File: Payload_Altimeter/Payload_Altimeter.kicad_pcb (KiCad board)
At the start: 2 copper layers, 80 x 93.6 mm, 6 parts, among them J1 L717SDC37P1ACH4F, J2 Conn_02x20_Odd_Even, U7 MS5607-02BA

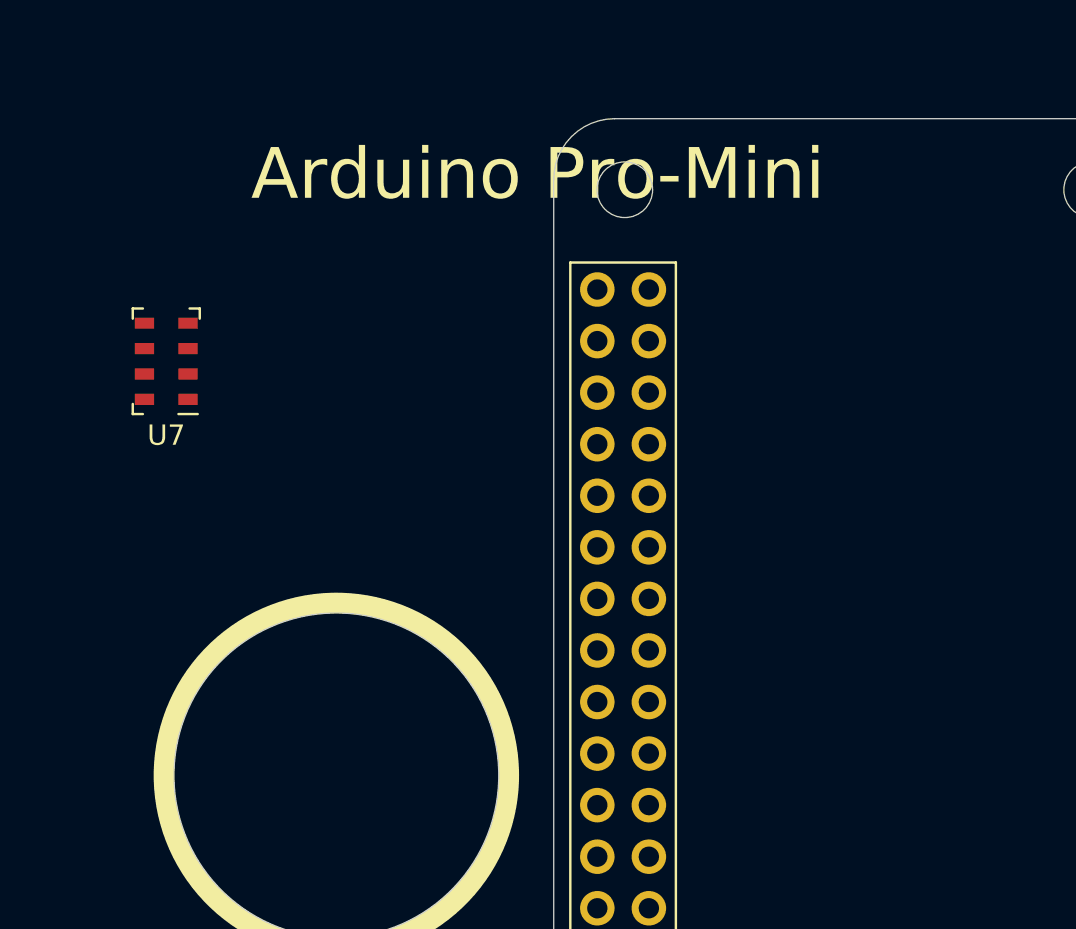
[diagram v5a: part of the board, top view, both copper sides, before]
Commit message: Some connection
Put some of the connections on but not all of them
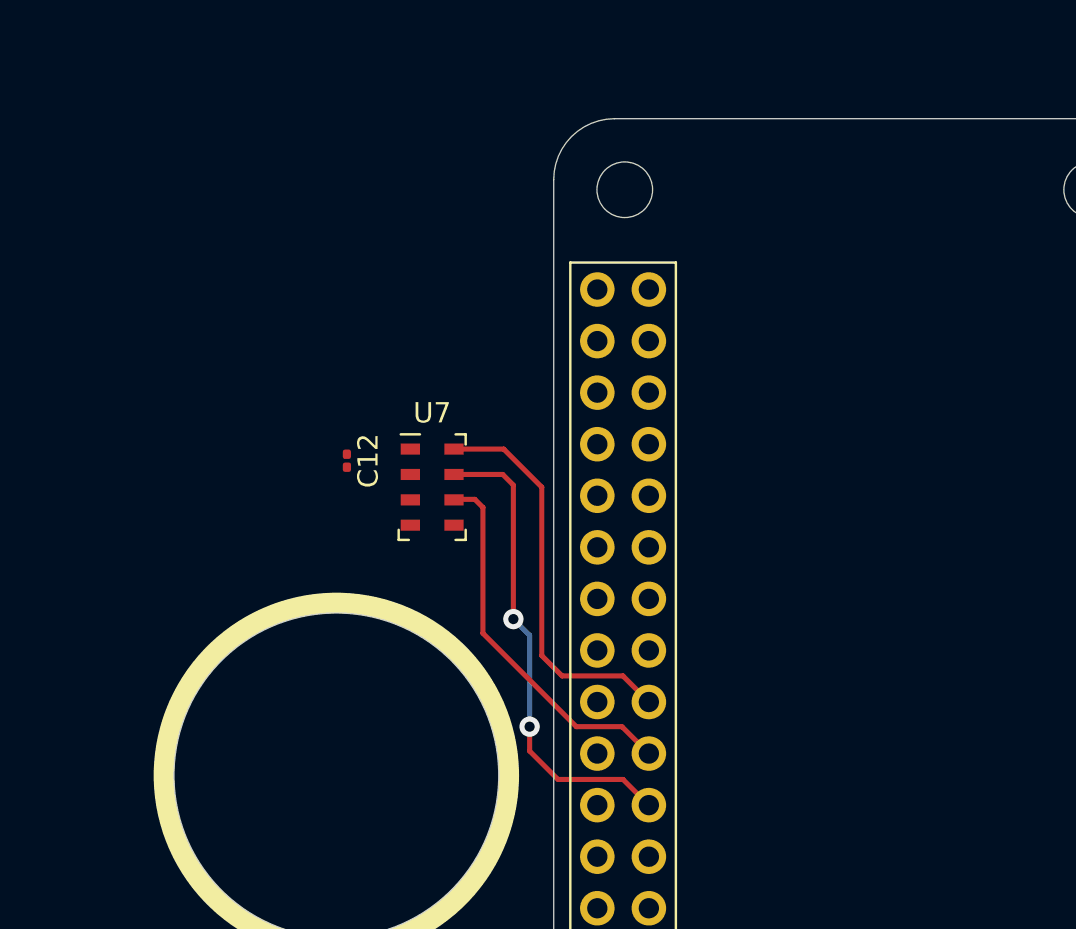
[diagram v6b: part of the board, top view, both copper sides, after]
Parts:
- added C12: 100nF, Capacitor_SMD:C_0201_0603Metric, F.Cu at (113.7, 81.3)
- J2: value Conn_02x20_Odd_Even -> Pi_Zero
- moved U7 14.5 mm to (117.9, 82.6), turned to 0 degrees
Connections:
- J2 pad 17: unconnected-(J2-Pad17) -> /Pi_3v3
- J2 pad 19: unconnected-(J2-Pad19) -> /MOSI
- J2 pad 2: unconnected-(J2-Pad2) -> +5V
- J2 pad 21: unconnected-(J2-Pad21) -> /MISO
- J2 pad 23: unconnected-(J2-Pad23) -> /SCLK
- J2 pad 4: unconnected-(J2-Pad4) -> +5V
- U7 pad 1: +3V3 -> /Pi_3v3
- U7 pad 4: /Altimeter/~{CSB} -> GND
- U7 pad 5: /Altimeter/~{CSB} -> GND
- U7 pad 6: /Altimeter/SDO -> /MISO
- U7 pad 7: /Altimeter/SDI_SDA -> /MOSI
- U7 pad 8: /Altimeter/SCLK -> /SCLK
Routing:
- net /MOSI: track 0.00 -> 23.6 mm, vias 0 -> 2
- net /SCLK: track 0.00 -> 19.6 mm
- net /MISO: track 0.00 -> 18.4 mm
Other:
- board text removed: "Arduino Pro-Mini"

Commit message: Finished PCB Layout
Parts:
- added 5V: 5V, TestPoint:TestPoint_Pad_D2.0mm, F.Cu at (121.1, 120.0)
- added GND: GND, TestPoint:TestPoint_Pad_D2.0mm, F.Cu at (99.4, 71.8)
- added MISO: MISO, TestPoint:TestPoint_Pad_D2.0mm, B.Cu at (140.8, 95.8)
- added MOSI: MOSI, TestPoint:TestPoint_Pad_D2.0mm, B.Cu at (140.8, 100.2)
- added Pi_3v3: Pi_3v3, TestPoint:TestPoint_Pad_D2.0mm, F.Cu at (120.8, 76.5)
- added SCLK: SCLK, TestPoint:TestPoint_Pad_D2.0mm, B.Cu at (140.8, 91.0)
- moved C12 1.30 mm to (115.0, 81.3)
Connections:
- J2 pad 14: unconnected-(J2-Pad14) -> GND
- J2 pad 20: unconnected-(J2-Pad20) -> GND
- J2 pad 25: unconnected-(J2-Pad25) -> GND
- J2 pad 30: unconnected-(J2-Pad30) -> GND
- J2 pad 34: unconnected-(J2-Pad34) -> GND
- J2 pad 39: unconnected-(J2-Pad39) -> GND
- J2 pad 6: unconnected-(J2-Pad6) -> GND
- J2 pad 9: unconnected-(J2-Pad9) -> GND
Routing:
- net +5V: track 0.00 -> 99.8 mm
- net /Pi_3v3: track 0.00 -> 44.0 mm
- net /SCLK: track 19.6 -> 32.7 mm
- net /MOSI: track 23.6 -> 36.6 mm
- net /MISO: track 18.4 -> 30.7 mm
- net GND: track 0.00 -> 8.48 mm, vias 0 -> 18
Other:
- outline, holes or cut-outs redrawn
